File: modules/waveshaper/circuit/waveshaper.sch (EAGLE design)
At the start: 17 parts, among them IC2 LM324N

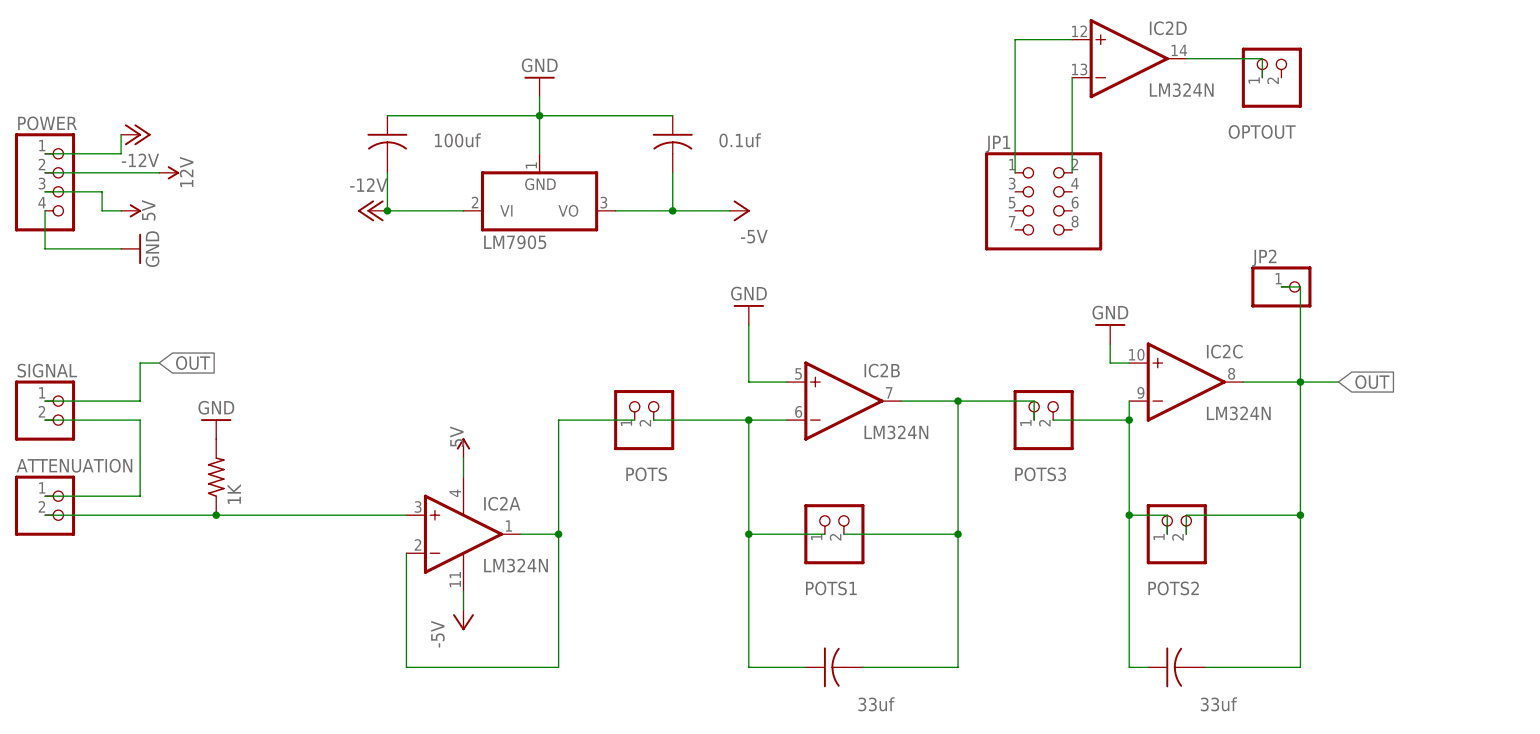
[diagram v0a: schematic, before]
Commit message: Adding resistors before each pots on wavshapper to avoid shorting when pot is at 0%
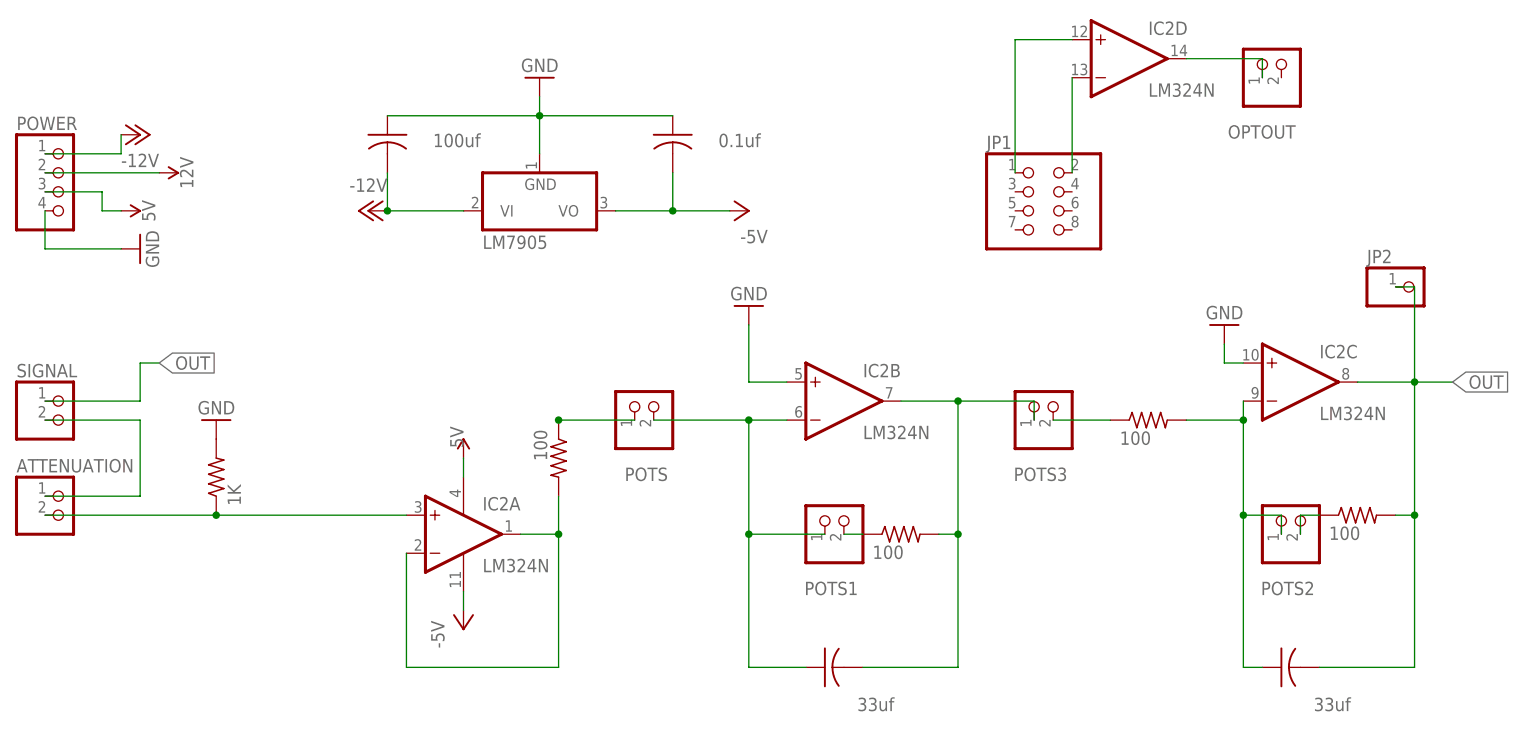
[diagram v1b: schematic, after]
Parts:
- added R2, R3, R4, R5: 100, adafruit:R-US_0207/12
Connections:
- new net N$10: POTS1.2, R3.1
- new net N$11: POTS2.2, R4.1
- new net N$12: POTS3.2, R5.1
- new net N$9: POTS.1, R2.1
- net N$3: now also R3.2; no longer POTS1.2
- net N$4: now also R5.2; no longer POTS3.2
- net N$8: now also R2.2; no longer POTS.1
- net OUT: now also R4.2; no longer POTS2.2
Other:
- moved on the sheet: IC2C, JP2, POTS2
